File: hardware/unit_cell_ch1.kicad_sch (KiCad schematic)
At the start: 5 parts, among them J1 Conn_RTD_4W

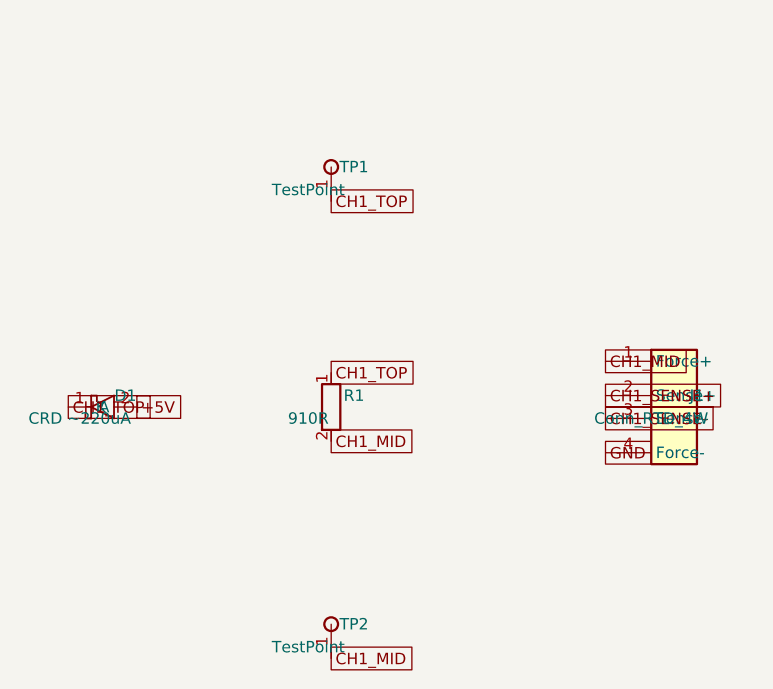
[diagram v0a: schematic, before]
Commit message: trackE: wire-up pass -- drawn wires + power symbols (netlist unchanged)
Convert the label-based capture to a conventionally drawn schematic: unit cells
as a drawn series current-loop (+5V/GND power symbols, CRD->R_ref->RTD, tapped
TOP/MID to TPs+labels); acquisition/power_io pins stub to power symbols/labels;
cross-sheet signals stay labelled. Fixed a y-down rotation bug (CRD anode/cathode
swap) by rotating the CRD 90 not 270.

ERC 0 errors / 0 warnings. Netlist node-for-node IDENTICAL to the pre-wiring
verified netlist (21 nets, diff empty); sim/netlists refreshed.

Co-Authored-By: Claude Opus 4.8 <noreply@anthropic.com>
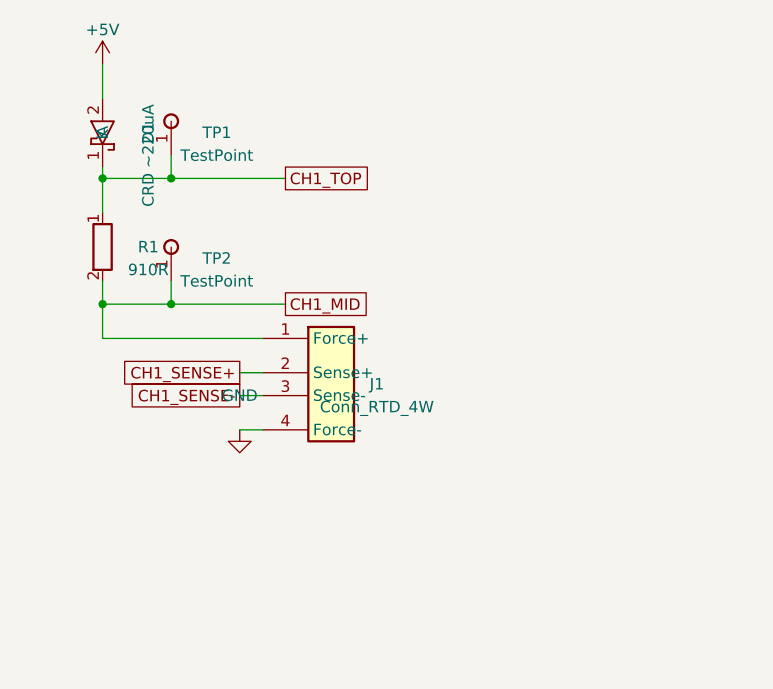
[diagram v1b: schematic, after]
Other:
- moved on the sheet: D1

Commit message: rev-B: real Digi-Key parts + layout review (copper unchanged)
Independent layout review + adversarial verify: 4-layer split planes, single-
point analog/digital GND tie, Kelvin intact -> fabricable (yes-with-fixes).
Real Digi-Key MPNs on the whole BOM; fixed RTD conn P/N (1729160 6-pos ->
1729144 4-pos) and R_ref tempco (25ppm -> Vishay TNPU1206 <=10ppm per spec).
ERC 0/0, DRC 0/0. Open decision: sense-line RC filter (see USER_MANUAL 8.5).

Co-Authored-By: Claude Opus 4.8 <noreply@anthropic.com>
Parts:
- J1: MPN 1729160 (MKDS 1,5/4-5,08) -> 1729144 (MKDS 1,5/4-5,08)
- R1: MPN RG3216P-911-B-T5 -> TNPU1206 910R 0.1% 10ppm (confirm code); Manufacturer Susumu (representative; any <=10 ppm/C thin-film ~910R is a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 -> Vishay (>=10ppm/C thin-film; see BOM_REVIEW)
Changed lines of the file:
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@@
 			)
 		)
-		(property "MPN" "RG3216P-911-B-T5"
+		(property "MPN" "TNPU1206 910R 0.1% 10ppm (confirm code)"
 			(at 50.8 45.72 0)
 			(show_name no)
@@
 			)
 		)
-		(property "Manufacturer" "Susumu (representative; any <=10 ppm/C thin-film ~910R is acceptable)"
+		(property "Manufacturer" "Vishay (>=10ppm/C thin-film; see BOM_REVIEW)"
 			(at 50.8 45.72 0)
 			(show_name no)
@@
 			)
 		)
-		(property "MPN" "1729160 (MKDS 1,5/4-5,08)"
+		(property "MPN" "1729144 (MKDS 1,5/4-5,08)"
 			(at 76.2 60.96 0)
 			(show_name no)
